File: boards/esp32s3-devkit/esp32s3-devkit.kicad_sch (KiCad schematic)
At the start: 37 parts, among them J1 Conn_01x17_Pin, J2 Conn_01x17_Pin, J3 USB_C_Receptacle_USB2.0_16P, Q1 Q_PMOS_GSD, SW1 MK-12C03-G015, SW2 RESET, SW3 BOOT, U1 TPS63070RNMR, U2 ESP32-S3-WROOM-1, U3 USBLC6-2SC6

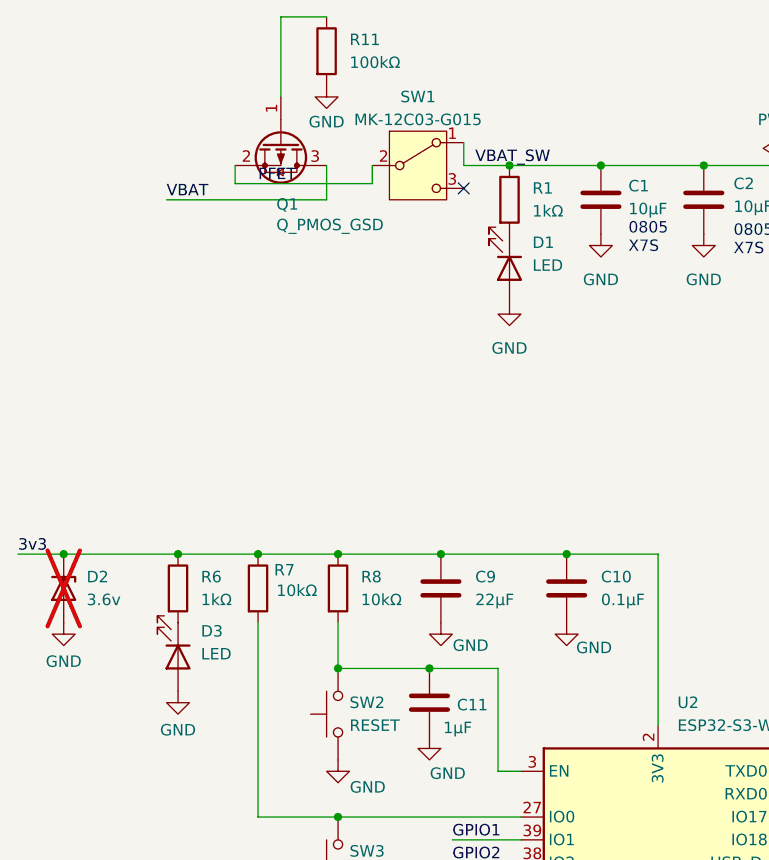
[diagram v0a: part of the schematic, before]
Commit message: fix(esp32s3-devkit): clear ERC/DRC warnings, fix LED polarity, correct fab files
- ERC: snap PFET wire run and net label from y=49.0 to on-grid y=49.53
  (3 off-grid endpoint warnings)
- DRC parity: add SH shield pin to the SW_SPDT symbol tied to GND so
  SW1's four shield pads match the schematic (4 net_conflict warnings)
- Fix reversed power LEDs D1 (VBAT_SW) and D3 (3V3): anodes were on GND
  so neither LED could ever light; flipped in schematic and rotated both
  footprints 180deg on the PCB (nets renamed Net-(Dx-K) -> Net-(Dx-A))
- Mark TPS63070 footprint as SMD (was through_hole) in board and library;
  it was silently dropped from the SMD position file, so JLCPCB would not
  have placed U1
- Regenerate JLCPCB CPL from the current layout (checked-in file was stale:
  positions/rotations predated the Q1 rewire; U1 row missing)
- Remove D2 from JLCPCB BOM: schematic marks it DNP / not in BOM

ERC, DRC (incl. schematic parity), and multi-fab DRC all pass locally.

Co-Authored-By: Claude Fable 5 <noreply@anthropic.com>
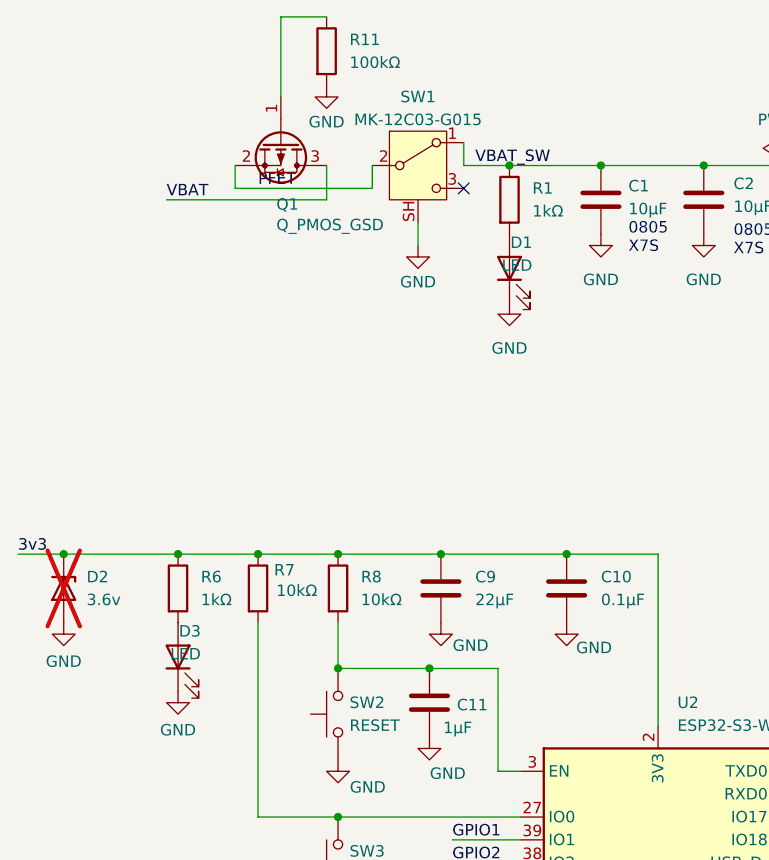
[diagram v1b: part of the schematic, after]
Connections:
- net GND: now also D1.1 (K), D3.1 (K), SW1.SH; no longer D1.2 (A), D3.2 (A)
- net at R6.2: now also D3.2 (A); no longer D3.1 (K)
- net at R1.2: now also D1.2 (A); no longer D1.1 (K)
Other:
- moved on the sheet: D1, D3
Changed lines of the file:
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@@
 	(wire
 		(pts
-			(xy 41.91 46.99) (xy 41.91 49.0)
+			(xy 41.91 46.99) (xy 41.91 49.53)
 		)
 		(stroke
@@
 	(wire
 		(pts
-			(xy 41.91 49.0) (xy 57.15 49.0)
+			(xy 41.91 49.53) (xy 57.15 49.53)
 		)
 		(stroke
@@
 	(wire
 		(pts
-			(xy 57.15 49.0) (xy 57.15 46.99)
+			(xy 57.15 49.53) (xy 57.15 46.99)
+		)
+		(stroke
+			(width 0)
+			(type default)
+		)
+	)
+	(wire
+		(pts
+			(xy 62.23 53.34) (xy 62.23 55.88)
 		)
 		(stroke
@@
 	)
 	(label "PFET"
-		(at 44.45 49.0 0)
+		(at 44.45 49.53 0)
 		(effects
 			(font
@@
 	)
 	(symbol
+		(lib_id "power:GND")
+		(at 62.23 55.88 0)
+		(unit 1)
+		(body_style 1)
+		(exclude_from_sim no)
+		(in_bom yes)
+		(on_board yes)
+		(in_pos_files yes)
+		(dnp no)
+		(property "Reference" "#PWR030"
+			(at 62.23 62.23 0)
+			(hide yes)
+			(show_name no)
+			(do_not_autoplace no)
+			(effects
+				(font
+					(size 1.27 1.27)
+				)
+			)
+		)
+		(property "Value" "GND"
+			(at 62.23 59.944 0)
+			(show_name no)
+			(do_not_autoplace no)
+			(effects
+				(font
+					(size 1.27 1.27)
+				)
+			)
+		)
+		(property "Footprint" ""
+			(at 62.23 55.88 0)
+			(hide yes)
+			(show_name no)
+			(do_not_autoplace no)
+			(effects
+				(font
+					(size 1.27 1.27)
+				)
+			)
+		)
+		(property "Datasheet" ""
+			(at 62.23 55.88 0)
+			(hide yes)
+			(show_name no)
+			(do_not_autoplace no)
+			(effects
+				(font
+					(size 1.27 1.27)
+				)
+			)
+		)
+		(property "Description" "Power symbol creates a global label with name \"GND\" , ground"
+			(at 62.23 55.88 0)
+			(hide yes)
+			(show_name no)
+			(do_not_autoplace no)
+			(effects
+				(font
+					(size 1.27 1.27)
+				)
+			)
+		)
+		(pin "1"
+		)
+		(instances
+			(project "esp32s3-devkit"
+				(path "/7924bd8b-2498-4d76-899d-c0ad5a514485"
+					(reference "#PWR030")
+					(unit 1)
+				)
+			)
+		)
+	)
+	(symbol
 		(lib_id "Device:R")
 		(at 35.56 93.98 0)
@@
 		(pin "3"
 		)
+		(pin "SH"
+		)
 		(instances
 			(project "esp32s3-devkit"
@@
 	(symbol
 		(lib_id "Device:LED")
-		(at 35.56 101.6 270)
+		(at 35.56 101.6 90)
 		(unit 1)
 		(body_style 1)
@@
 	(symbol
 		(lib_id "Device:LED")
-		(at 72.39 58.42 270)
+		(at 72.39 58.42 90)
 		(unit 1)
 		(body_style 1)

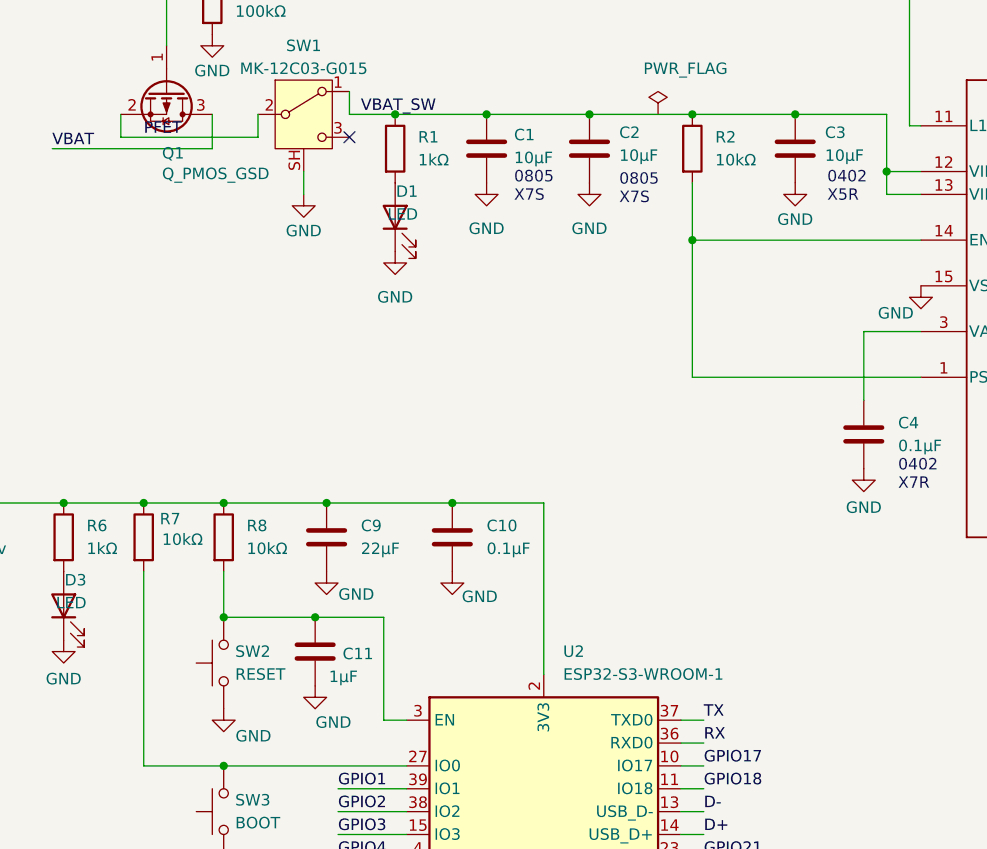
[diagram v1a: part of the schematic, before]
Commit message: test(esp32s3-devkit): add design validation, battery-range SPICE, and bring-up plan
Board-level test coverage for the battery-powered devkit ahead of fab:

- checks.yml: design-intent validation (make validate) — pins all 31
  components incl. Q1=AO3401A and U2=ESP32-S3-WROOM-1-N16 (values aligned
  with the JLCPCB BOM), required nets, input/output capacitance budgets,
  BOM hygiene, and the TPS63070 FB divider math (0.8V ref, 3.3V ±2% —
  guards the exact fixed-vs-adjustable bug PR #107 fixed)
- sim.yml + sim/: opt-in SPICE (make sim-board / CI spice-board) sweeping
  the 3xAA range 4.8V -> 3.6V (buck-boost transition) -> 3.0V (end-of-life)
  with 0.5A WiFi-TX load bursts, plus a cold-start-at-3.0V secondary pass;
  13 bounded measures with committed baseline. The TI model is quasi-ideal
  (documented in sim.yml), so these act as topology regressions — a
  miswired divider or dead rail fails loudly
- schematic: add Sim.* subckt mapping to U1 instance; exclude non-electrical
  parts (module, USB, switches, LEDs, PMOS, connectors) from simulation;
  footprint_symbol_field_mismatch set to ignore to match the breakout's
  convention for symbol-only Sim fields
- docs/bringup.md: bench-test checklist for first articles — smoke checks,
  reverse-battery, brown-out sweep, USB flashing on battery (incl. weak-pack
  boot strapping), WiFi soak on tired cells, deep-sleep current record
- tests: sim discovery now expects esp32s3-devkit to be opted in

make validate, make check, and the full SPICE suite pass locally.

Co-Authored-By: Claude Fable 5 <noreply@anthropic.com>
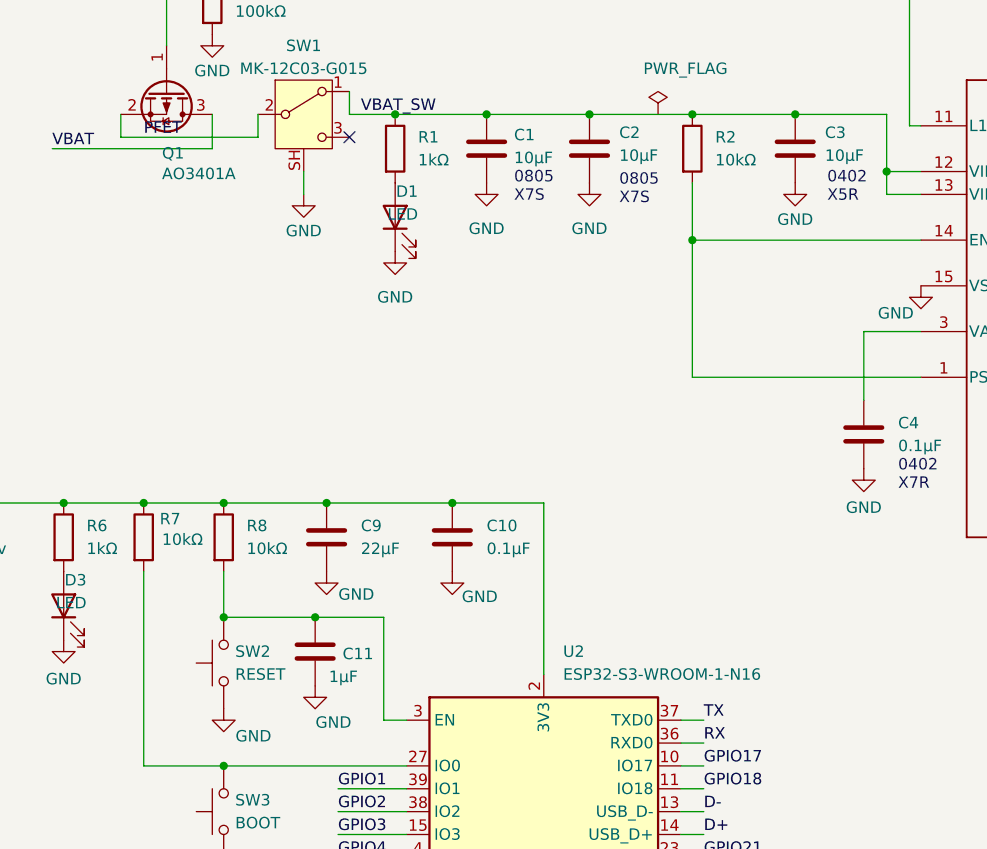
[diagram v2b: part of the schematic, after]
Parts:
- Q1: value Q_PMOS_GSD -> AO3401A
- U2: value ESP32-S3-WROOM-1 -> ESP32-S3-WROOM-1-N16
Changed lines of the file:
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@@
 		(unit 1)
 		(body_style 1)
-		(exclude_from_sim no)
+		(exclude_from_sim yes)
 		(in_bom no)
 		(on_board yes)
@@
 		(unit 1)
 		(body_style 1)
-		(exclude_from_sim no)
+		(exclude_from_sim yes)
 		(in_bom yes)
 		(on_board yes)
@@
 		(unit 1)
 		(body_style 1)
-		(exclude_from_sim no)
+		(exclude_from_sim yes)
 		(in_bom yes)
 		(on_board yes)
@@
 		(unit 1)
 		(body_style 1)
-		(exclude_from_sim no)
+		(exclude_from_sim yes)
 		(in_bom yes)
 		(on_board yes)
@@
 			)
 		)
-		(property "Value" "ESP32-S3-WROOM-1"
+		(property "Value" "ESP32-S3-WROOM-1-N16"
 			(at 91.0433 109.22 0)
 			(show_name no)
@@
 		(unit 1)
 		(body_style 1)
-		(exclude_from_sim no)
+		(exclude_from_sim yes)
 		(in_bom yes)
 		(on_board yes)
@@
 		(unit 1)
 		(body_style 1)
-		(exclude_from_sim no)
+		(exclude_from_sim yes)
 		(in_bom yes)
 		(on_board yes)
@@
 		(unit 1)
 		(body_style 1)
-		(exclude_from_sim no)
+		(exclude_from_sim yes)
 		(in_bom yes)
 		(on_board yes)
@@
 		(unit 1)
 		(body_style 1)
-		(exclude_from_sim no)
+		(exclude_from_sim yes)
 		(in_bom yes)
 		(on_board yes)
@@
 			)
 		)
+		(property "Sim.Type" "SUBCKT"
+			(at 151.13 68.58 0)
+			(hide yes)
+			(show_name no)
+			(do_not_autoplace no)
+			(effects
+				(font
+					(size 1.27 1.27)
+				)
+			)
+		)
+		(property "Sim.Name" "TPS63070_TRANS"
+			(at 151.13 68.58 0)
+			(hide yes)
+			(show_name no)
+			(do_not_autoplace no)
+			(effects
+				(font
+					(size 1.27 1.27)
+				)
+			)
+		)
+		(property "Sim.Pins" "1=PS_SYNC 2=PG 3=VAUX 4=GND 5=FB 6=FB2 7=VOUT_0 8=VOUT_1 9=L2 10=PGND 11=L1 12=VIN_0 13=VIN_1 14=EN 15=VSEL"
+			(at 151.13 68.58 0)
+			(hide yes)
+			(show_name no)
+			(do_not_autoplace no)
+			(effects
+				(font
+					(size 1.27 1.27)
+				)
+			)
+		)
+		(property "Sim.Library" "../../libs/spice/tps63070/TPS63070_TRANS.LIB"
+			(at 151.13 68.58 0)
+			(hide yes)
+			(show_name no)
+			(do_not_autoplace no)
+			(effects
+				(font
+					(size 1.27 1.27)
+				)
+			)
+		)
 		(pin "15"
 		)
@@
 		(unit 1)
 		(body_style 1)
-		(exclude_from_sim no)
+		(exclude_from_sim yes)
 		(in_bom yes)
 		(on_board yes)
@@
 		(unit 1)
 		(body_style 1)
-		(exclude_from_sim no)
+		(exclude_from_sim yes)
 		(in_bom yes)
 		(on_board yes)
@@
 		(unit 1)
 		(body_style 1)
-		(exclude_from_sim no)
+		(exclude_from_sim yes)
 		(in_bom yes)
 		(on_board yes)
@@
 			)
 		)
-		(property "Value" "Q_PMOS_GSD"
+		(property "Value" "AO3401A"
 			(at 46.482 53.594 90)
 			(show_name no)
@@
 		(unit 1)
 		(body_style 1)
-		(exclude_from_sim no)
+		(exclude_from_sim yes)
 		(in_bom yes)
 		(on_board yes)
@@
 		(unit 1)
 		(body_style 1)
-		(exclude_from_sim no)
+		(exclude_from_sim yes)
 		(in_bom yes)
 		(on_board yes)

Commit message: fix(esp32s3-devkit): retarget SW2/SW3 to TS-1187A footprint for JLC assembly (#115)
The RESET/BOOT buttons used Button_Switch_SMD:SW_SPST_TL3342, which does
not correspond to a JLCPCB-stocked tactile switch — JLC auto-matched it to
TS-1187A (C318884, their Basic go-to) but flagged it because the TL3342
footprint (pads at +/-3.15mm X, +/-1.90mm Y) does not fit the 5.1mm part,
so the buttons could not be placed.

Swap both to Button_Switch_SMD:SW_Push_1P1T_XKB_TS-1187A, the footprint
made for that exact part. Pad centers move <=0.15mm (+/-3.00mm / +/-1.88mm)
and pad numbering/nets are preserved, so routing is unchanged; ERC, DRC,
schematic parity, fab-DRC, and validate all pass. JLC now matches C318884
cleanly and assembles the buttons.

Co-authored-by: Claude Fable 5 <noreply@anthropic.com>
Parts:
- SW2, SW3: footprint Button_Switch_SMD:SW_SPST_TL3342 -> Button_Switch_SMD:SW_Push_1P1T_XKB_TS-1187A
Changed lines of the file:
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@@
 			)
 		)
-		(property "Footprint" "Button_Switch_SMD:SW_SPST_TL3342"
+		(property "Footprint" "Button_Switch_SMD:SW_Push_1P1T_XKB_TS-1187A"
 			(at 48.26 107.95 0)
 			(hide yes)
@@
 			)
 		)
-		(property "Footprint" "Button_Switch_SMD:SW_SPST_TL3342"
+		(property "Footprint" "Button_Switch_SMD:SW_Push_1P1T_XKB_TS-1187A"
 			(at 48.26 124.46 0)
 			(hide yes)
